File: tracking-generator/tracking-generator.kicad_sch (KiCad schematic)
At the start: 32 parts, among them J1 SA VCO, Q1 MPSH81, Q2 NPN, Q3 NPN, U1 NE602

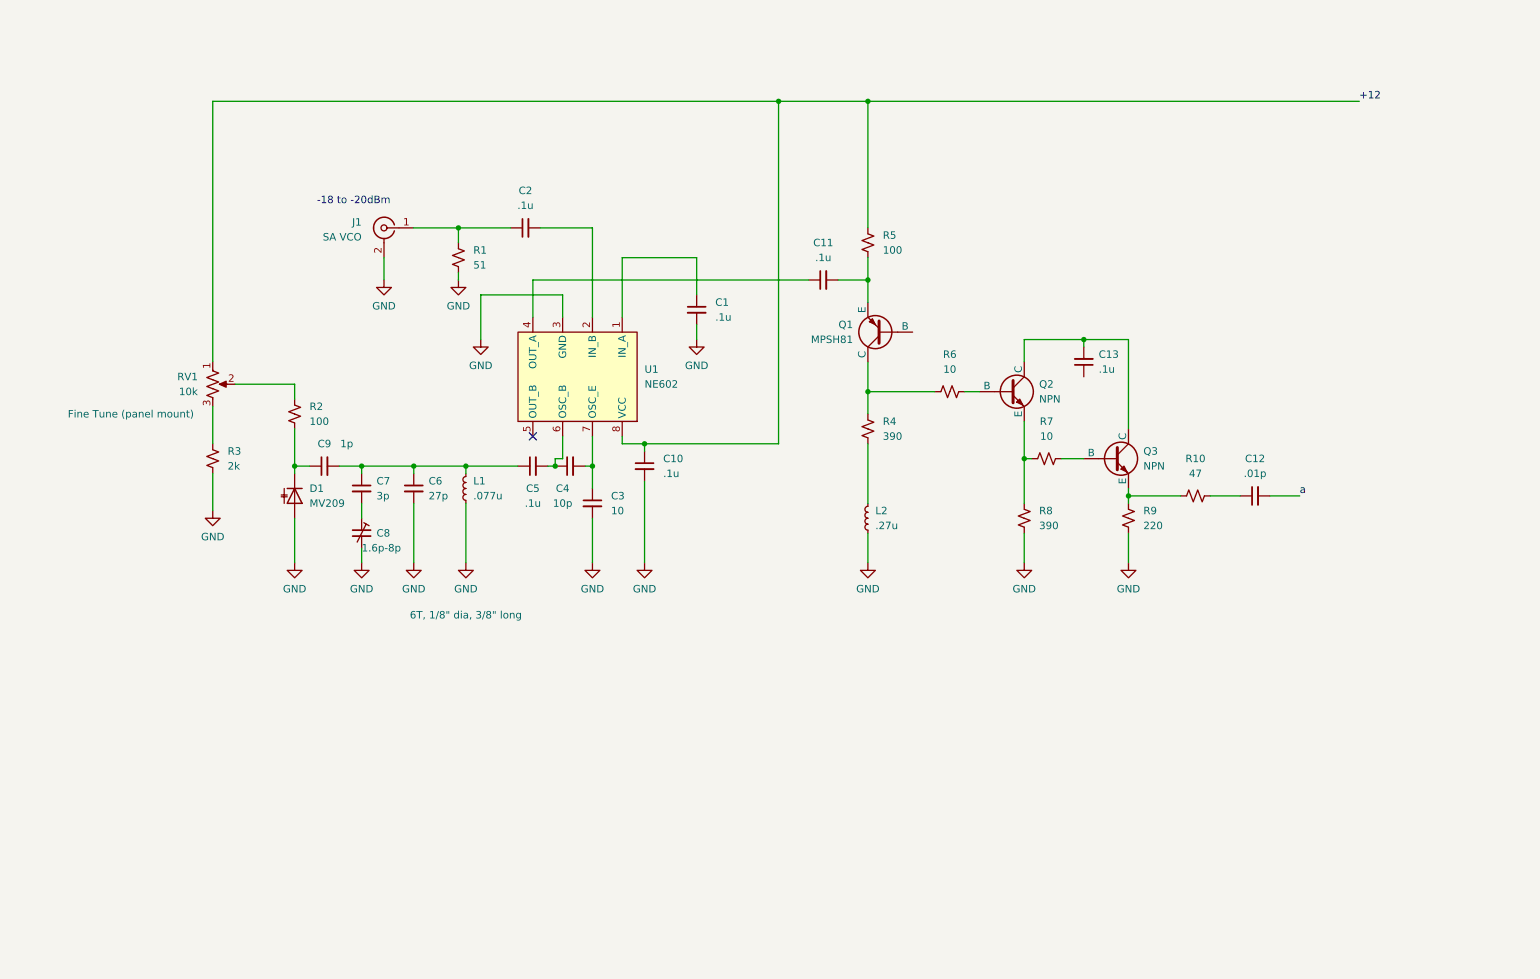
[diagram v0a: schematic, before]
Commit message: adding +6V section of tracking-generator
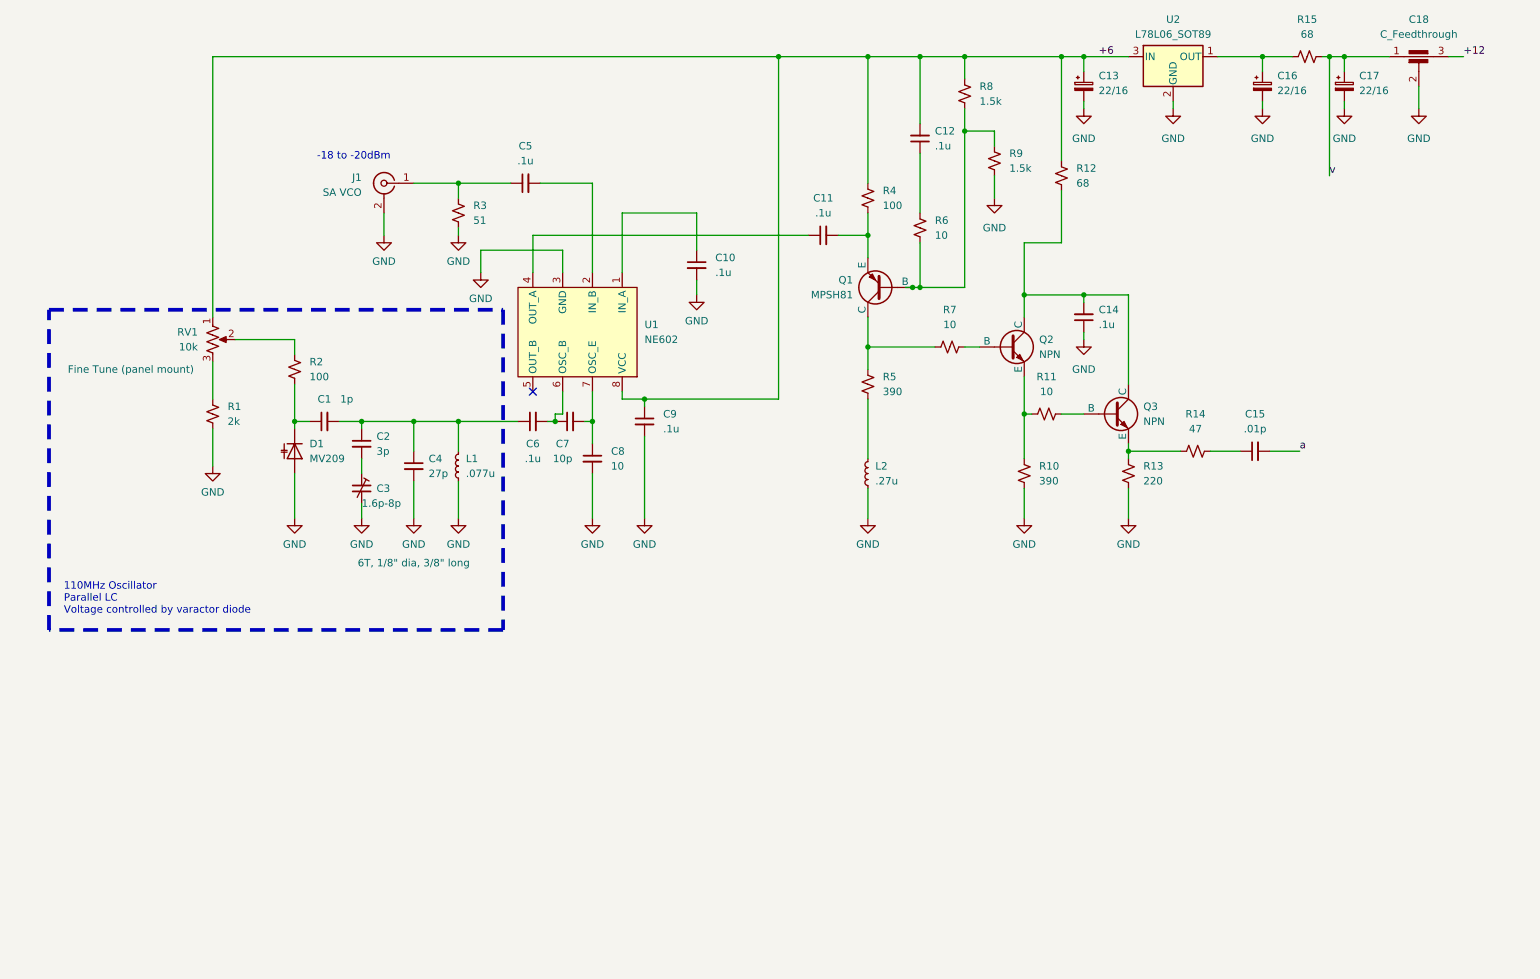
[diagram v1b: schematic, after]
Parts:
- added C12: .1u, symbol Device:C_Small
- added C13, C16, C17: 22/16, symbol Device:C_Polarized_Small
- added C18: C_Feedthrough, symbol Device:C_Feedthrough
- added R12, R15: 68, symbol Device:R_Small_US
- added R6: 10, symbol Device:R_Small_US
- added R8, R9: 1.5k, symbol Device:R_Small_US
- added U2: L78L06_SOT89, Package_TO_SOT_SMD:SOT-89-3, symbol Regulator_Linear:L78L06_SOT89
- renumbered C9 to C1, C1 to C10, C13 to C14, C12 to C15, C7 to C2, C8 to C3, C6 to C4, C2 to C5, C5 to C6, C4 to C7, C3 to C8, C10 to C9, R3 to R1, R8 to R10, R7 to R11, R9 to R13, R10 to R14, R1 to R3, R5 to R4, R4 to R5, R6 to R7
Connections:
- net +12: now also C18.3; no longer C9.1, R4.1, RV1.1, U1.8 (VCC)
- net GND: now also C14.1, C13.2, C16.2, C17.2, C18.2, R9.2, U2.2 (GND)
- net at C14.2, Q2.1 (C), Q3.1 (C): now also R12.2
- net at Q1.2 (B): now also R6.2, R8.2, R9.1
- new net: C12.1, R6.1
- new net: C16.1, R15.2, U2.1 (OUT)
- new net +6: C12.2, C13.1, C9.1, R12.1, R4.1, R8.1, RV1.1, U1.8 (VCC), U2.3 (IN)
- new net v: C17.1, C18.1, R15.1
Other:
- note added: "110MHz Oscillator Parallel LC Voltage controlled by varactor diode"
- title: Tracking Generator -> K3NHI/K5IRK Tracking Generator
- moved on the sheet: C1, C10, C11, C14, C15, C2, C3, C4, C5, C6, C7, C8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

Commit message: tracking-generator amplifier stage added
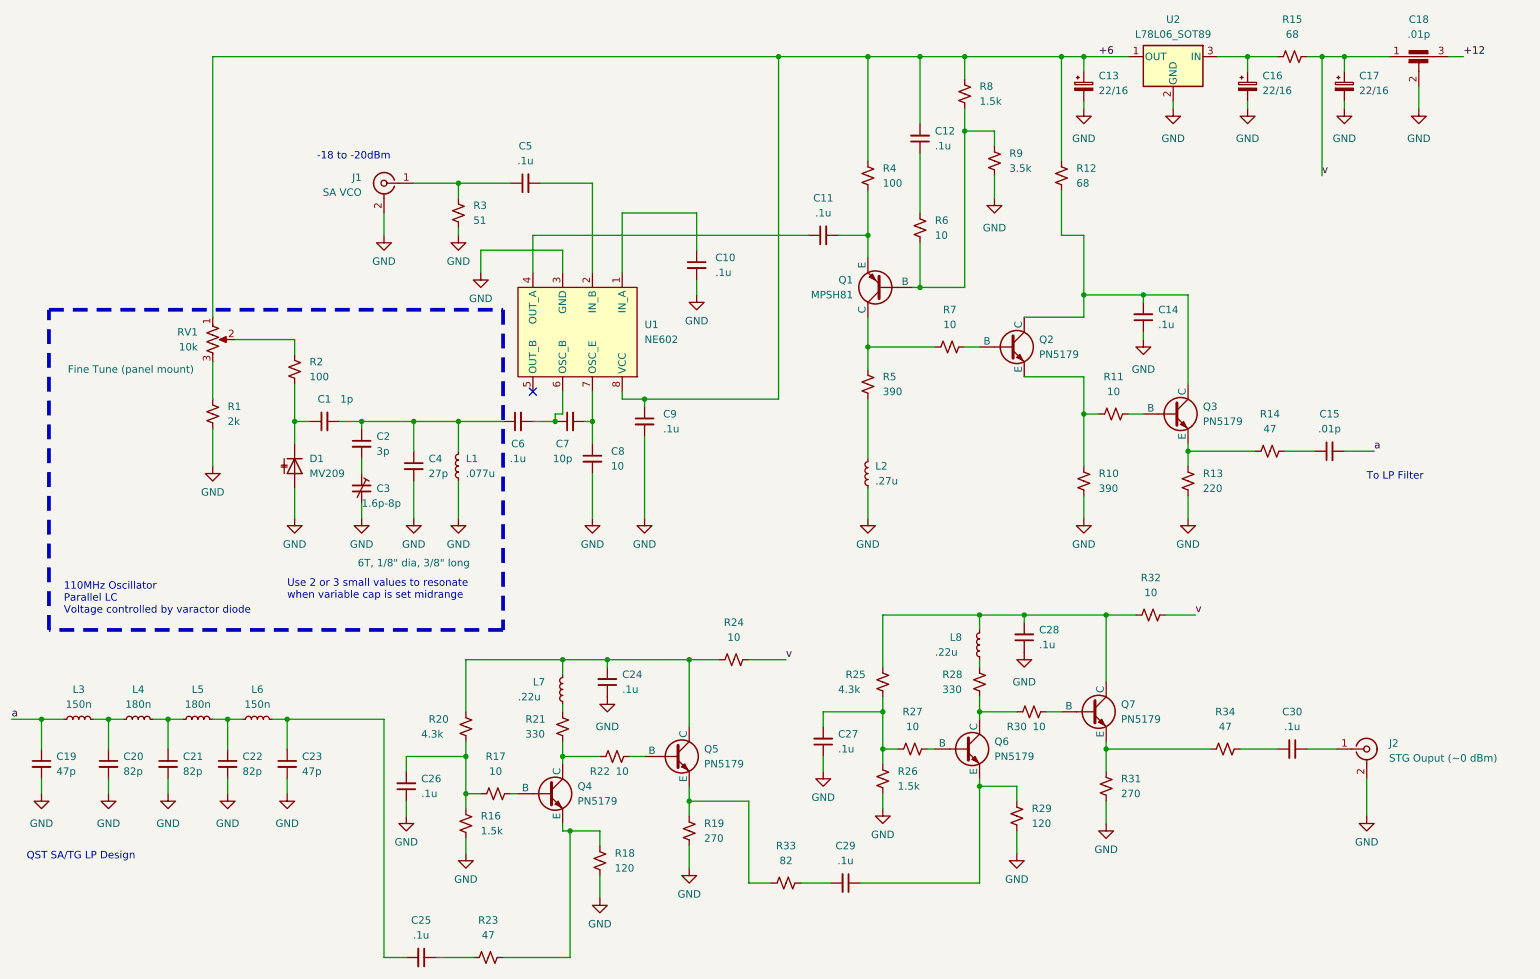
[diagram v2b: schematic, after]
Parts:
- added C19, C23: 47p, Capacitor_SMD:C_0603_1608Metric_Pad1.08x0.95mm_HandSolder, symbol Device:C_Small
- added C20, C21, C22: 82p, Capacitor_SMD:C_0603_1608Metric_Pad1.08x0.95mm_HandSolder, symbol Device:C_Small
- added C24, C25, C26, C27, C28, C29, C30: .1u, symbol Device:C_Small
- added J2: STG Ouput (~0 dBm), symbol Connector:Conn_Coaxial
- added L3, L6: 150n, Inductor_SMD:L_0603_1608Metric_Pad1.05x0.95mm_HandSolder, symbol Device:L_Small
- added L4, L5: 180n, Inductor_SMD:L_0603_1608Metric_Pad1.05x0.95mm_HandSolder, symbol Device:L_Small
- added L7, L8: .22u, symbol Device:L_Small
- added Q4, Q5, Q6, Q7: PN5179, symbol Simulation_SPICE:NPN
- added R16, R26: 1.5k, symbol Device:R_Small_US
- added R17, R22, R24, R27, R30, R32: 10, symbol Device:R_Small_US
- added R18, R29: 120, symbol Device:R_Small_US
- added R19, R31: 270, symbol Device:R_Small_US
- added R20, R25: 4.3k, symbol Device:R_Small_US
- added R21, R28: 330, symbol Device:R_Small_US
- added R23, R34: 47, symbol Device:R_Small_US
- added R33: 82, symbol Device:R_Small_US
- C18: value C_Feedthrough -> .01p
- Q2, Q3: value NPN -> PN5179
- R9: value 1.5k -> 3.5k
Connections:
- net +6: now also U2.1 (OUT); no longer U2.3 (IN)
- net GND: now also C19.2, C20.2, C21.2, C22.2, C23.2, C24.1, C26.1, C27.1, C28.1, J2.2 (Ext), R16.2, R18.2, R19.2, R26.2, R29.2, R31.2
- net a: now also C19.1, L3.1
- net v: now also R24.1, R32.1
- net at C16.1, R15.2: now also U2.3 (IN); no longer U2.1 (OUT)
- new net: C23.1, C25.2, L6.2
- new net: C20.1, L3.2, L4.1
- new net: C26.2, R16.1, R17.2, R20.2
- new net: C22.1, L5.2, L6.1
- new net: Q7.3 (E), R31.1, R34.2
- new net: C29.2, R33.1
- new net: Q5.3 (E), R19.1, R33.2
- new net: Q4.3 (E), R18.1, R23.1
- new net: C30.2, R34.1
- new net: Q5.2 (B), R22.1
- new net: Q4.1 (C), R21.2, R22.2
- new net: L8.1, R28.1
- new net: C28.2, L8.2, Q7.1 (C), R25.1, R32.2
- new net: Q6.1 (C), R28.2, R30.2
- new net: C30.1, J2.1 (In)
- new net: C24.2, L7.2, Q5.1 (C), R20.1, R24.2
- new net: C27.2, R25.2, R26.1, R27.2
- new net: C21.1, L4.2, L5.1
- new net: Q4.2 (B), R17.1
- new net: C29.1, Q6.3 (E), R29.1
- new net: Q7.2 (B), R30.1
- new net: Q6.2 (B), R27.1
- new net: L7.1, R21.1
- new net: C25.1, R23.2
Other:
- note added: "QST SA/TG LP Design"
- note added: "To LP Filter"
- note added: "Use 2 or 3 small values to resonate when variable cap is set midrange"
- moved on the sheet: C14, C15, C16, C6, D1, Q3, R10, R11, R13, R14, R15, R4
